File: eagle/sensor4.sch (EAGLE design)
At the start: 16 parts, among them X1 1503_02, X3 1503_02

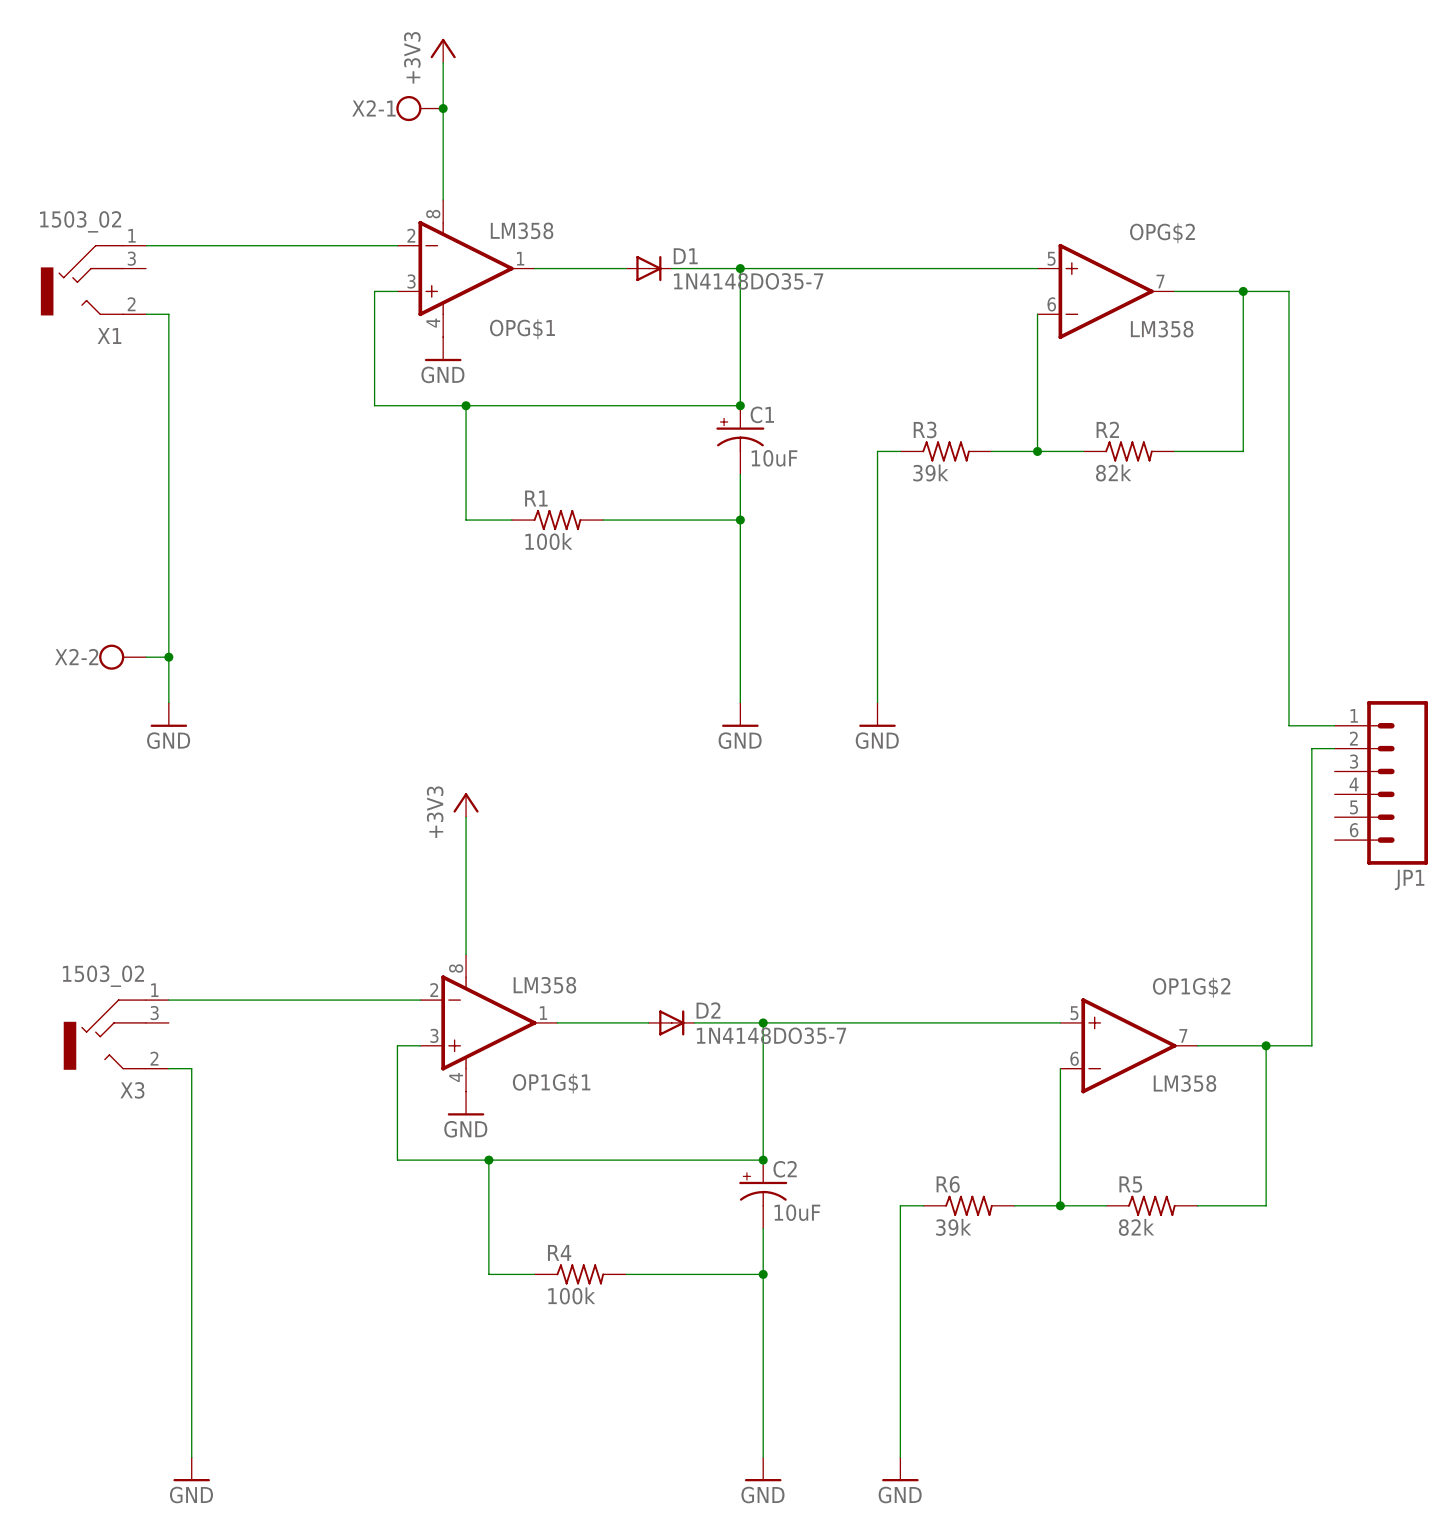
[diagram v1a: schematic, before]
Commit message: Replace two LM358s with one LMV324
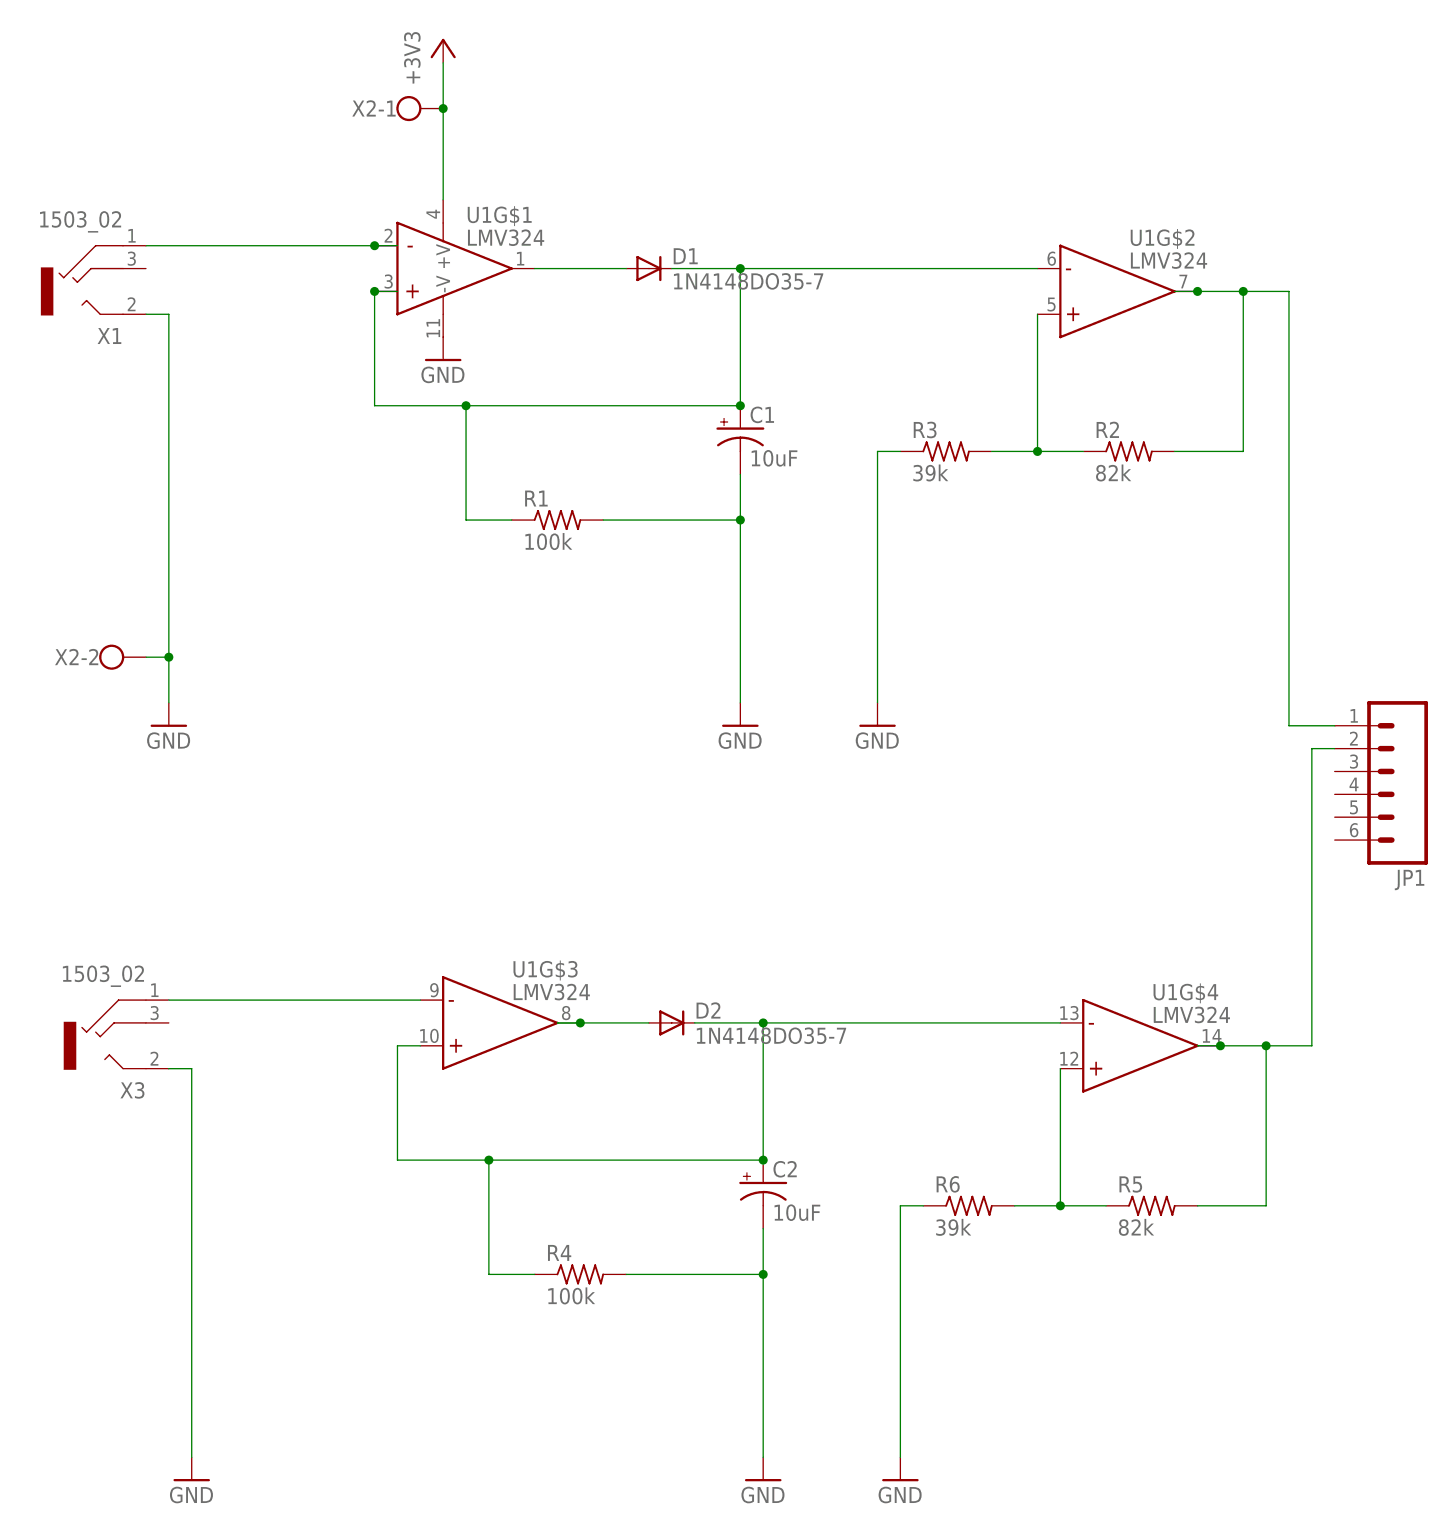
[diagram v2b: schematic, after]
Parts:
- removed OP, OP1: LM358, SparkFun-AnalogIC:LM358
- added U1: LMV324, SparkFun-AnalogIC:LMV324
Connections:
- net +3V3: now also U1G$1.+V; no longer OP1G$1.V+, OPG$1.V+
- net GND: now also U1G$1.-V; no longer OP1G$1.V-, OPG$1.V-
- net N$1: now also U1G$1.OUT; no longer OPG$1.OUT
- net N$10: now also U1G$4.OUT; no longer OP1G$2.OUT
- net N$2: now also U1G$1.+IN, U1G$2.-IN; no longer OPG$1.+IN, OPG$2.+IN
- net N$3: now also U1G$3.OUT; no longer OP1G$1.OUT
- net N$4: now also U1G$3.+IN, U1G$4.-IN; no longer OP1G$1.+IN, OP1G$2.+IN
- net N$5: now also U1G$2.+IN; no longer OPG$2.-IN
- net N$6: now also U1G$1.-IN; no longer OPG$1.-IN
- net N$7: now also U1G$2.OUT; no longer OPG$2.OUT
- net N$8: now also U1G$4.+IN; no longer OP1G$2.-IN
- net N$9: now also U1G$3.-IN; no longer OP1G$1.-IN
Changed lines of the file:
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@@
 </classes>
 <parts>
-<part name="OP" library="SparkFun-AnalogIC" deviceset="LM358" device=""/>
 <part name="C1" library="resistor" deviceset="CPOL-US" device="E2.5-5" value="10uF"/>
 <part name="R1" library="resistor" deviceset="R-US_" device="0207/10" value="100k"/>
@@
 <part name="GND4" library="supply1" deviceset="GND" device=""/>
 <part name="X1" library="con-lumberg" deviceset="1503_02" device=""/>
-<part name="OP1" library="SparkFun-AnalogIC" deviceset="LM358" device=""/>
 <part name="C2" library="resistor" deviceset="CPOL-US" device="E2.5-5" value="10uF"/>
 <part name="R4" library="resistor" deviceset="R-US_" device="0207/10" value="100k"/>
@@
 <part name="R6" library="resistor" deviceset="R-US_" device="0207/10" value="39k"/>
 <part name="D2" library="diode" deviceset="1N4148" device="DO35-7"/>
-<part name="+3V1" library="supply1" deviceset="+3V3" device=""/>
 <part name="GND5" library="supply1" deviceset="GND" device=""/>
 <part name="GND6" library="supply1" deviceset="GND" device=""/>
-<part name="GND7" library="supply1" deviceset="GND" device=""/>
 <part name="GND8" library="supply1" deviceset="GND" device=""/>
 <part name="X3" library="con-lumberg" deviceset="1503_02" device=""/>
 <part name="X2" library="con-wago-500" deviceset="W237-102" device=""/>
 <part name="JP1" library="SparkFun-Connectors" deviceset="M06" device="SIP"/>
+<part name="U1" library="SparkFun-AnalogIC" deviceset="LMV324" device="" value="LMV324"/>
 </parts>
 <sheets>
@@
 </plain>
 <instances>
-<instance part="OP" gate="G$1" x="43.18" y="71.12"/>
-<instance part="OP" gate="G$2" x="116.84" y="68.58"/>
 <instance part="C1" gate="G$1" x="76.2" y="53.34"/>
 <instance part="R1" gate="G$1" x="55.88" y="43.18"/>
@@
 <instance part="GND4" gate="1" x="12.7" y="20.32"/>
 <instance part="X1" gate="G$1" x="5.08" y="68.58" rot="R180"/>
-<instance part="OP1" gate="G$1" x="45.72" y="-12.7"/>
-<instance part="OP1" gate="G$2" x="119.38" y="-15.24"/>
 <instance part="C2" gate="G$1" x="78.74" y="-30.48"/>
 <instance part="R4" gate="G$1" x="58.42" y="-40.64"/>
@@
 <instance part="R6" gate="G$1" x="101.6" y="-33.02"/>
 <instance part="D2" gate="G$1" x="68.58" y="-12.7"/>
-<instance part="+3V1" gate="G$1" x="45.72" y="12.7"/>
 <instance part="GND5" gate="1" x="78.74" y="-63.5"/>
 <instance part="GND6" gate="1" x="93.98" y="-63.5"/>
-<instance part="GND7" gate="1" x="45.72" y="-22.86"/>
 <instance part="GND8" gate="1" x="15.24" y="-63.5"/>
 <instance part="X3" gate="G$1" x="7.62" y="-15.24" rot="R180"/>
@@
 <instance part="X2" gate="-2" x="5.08" y="27.94"/>
 <instance part="JP1" gate="G$1" x="147.32" y="15.24" rot="R180"/>
+<instance part="U1" gate="G$1" x="38.1" y="71.12"/>
+<instance part="U1" gate="G$2" x="111.76" y="68.58"/>
+<instance part="U1" gate="G$3" x="43.18" y="-12.7"/>
+<instance part="U1" gate="G$4" x="114.3" y="-15.24"/>
 </instances>
 <busses>
@@
 <nets>
 <net name="GND" class="0">
-<segment>
-<pinref part="OP" gate="G$1" pin="V-"/>
-<pinref part="GND3" gate="1" pin="GND"/>
-</segment>
 <segment>
 <pinref part="R1" gate="G$1" pin="2"/>
@@
 </segment>
 <segment>
-<pinref part="OP1" gate="G$1" pin="V-"/>
-<pinref part="GND7" gate="1" pin="GND"/>
-</segment>
-<segment>
 <pinref part="R4" gate="G$1" pin="2"/>
 <wire x1="63.5" y1="-40.64" x2="78.74" y2="-40.64" width="0.1524" layer="91"/>
@@
 <pinref part="X3" gate="G$1" pin="2"/>
 </segment>
+<segment>
+<pinref part="GND3" gate="1" pin="GND"/>
+<pinref part="U1" gate="G$1" pin="-V"/>
+</segment>
 </net>
 <net name="N$1" class="0">
 <segment>
-<pinref part="OP" gate="G$1" pin="OUT"/>
 <pinref part="D1" gate="G$1" pin="A"/>
 <wire x1="53.34" y1="71.12" x2="63.5" y2="71.12" width="0.1524" layer="91"/>
+<pinref part="U1" gate="G$1" pin="OUT"/>
 </segment>
 </net>
@@
 <wire x1="45.72" y1="55.88" x2="35.56" y2="55.88" width="0.1524" layer="91"/>
 <wire x1="35.56" y1="55.88" x2="35.56" y2="68.58" width="0.1524" layer="91"/>
-<pinref part="OP" gate="G$1" pin="+IN"/>
 <wire x1="35.56" y1="68.58" x2="38.1" y2="68.58" width="0.1524" layer="91"/>
 <pinref part="R1" gate="G$1" pin="1"/>
@@
 <junction x="76.2" y="71.12"/>
 <junction x="76.2" y="55.88"/>
-<pinref part="OP" gate="G$2" pin="+IN"/>
 <wire x1="76.2" y1="71.12" x2="109.22" y2="71.12" width="0.1524" layer="91"/>
+<pinref part="U1" gate="G$1" pin="+IN"/>
+<junction x="35.56" y="68.58"/>
+<pinref part="U1" gate="G$2" pin="-IN"/>
 </segment>
 </net>
@@
 <pinref part="R3" gate="G$1" pin="2"/>
 <wire x1="114.3" y1="50.8" x2="109.22" y2="50.8" width="0.1524" layer="91"/>
-<pinref part="OP" gate="G$2" pin="-IN"/>
 <wire x1="109.22" y1="50.8" x2="104.14" y2="50.8" width="0.1524" layer="91"/>
 <wire x1="109.22" y1="66.04" x2="109.22" y2="50.8" width="0.1524" layer="91"/>
 <junction x="109.22" y="50.8"/>
+<pinref part="U1" gate="G$2" pin="+IN"/>
 </segment>
 </net>
 <net name="+3V3" class="0">
 <segment>
-<pinref part="OP" gate="G$1" pin="V+"/>
 <pinref part="+3V2" gate="G$1" pin="+3V3"/>
 <wire x1="43.18" y1="78.74" x2="43.18" y2="88.9" width="0.1524" layer="91"/>
@@
 <wire x1="43.18" y1="88.9" x2="43.18" y2="93.98" width="0.1524" layer="91"/>
 <junction x="43.18" y="88.9"/>
-</segment>
-<segment>
-<pinref part="OP1" gate="G$1" pin="V+"/>
-<pinref part="+3V1" gate="G$1" pin="+3V3"/>
-<wire x1="45.72" y1="-5.08" x2="45.72" y2="10.16" width="0.1524" layer="91"/>
+<pinref part="U1" gate="G$1" pin="+V"/>
 </segment>
 </net>
 <net name="N$6" class="0">
 <segment>
-<pinref part="OP" gate="G$1" pin="-IN"/>
-<wire x1="10.16" y1="73.66" x2="38.1" y2="73.66" width="0.1524" layer="91"/>
+<wire x1="10.16" y1="73.66" x2="35.56" y2="73.66" width="0.1524" layer="91"/>
 <pinref part="X1" gate="G$1" pin="1"/>
+<pinref part="U1" gate="G$1" pin="-IN"/>
+<wire x1="35.56" y1="73.66" x2="38.1" y2="73.66" width="0.1524" layer="91"/>
+<junction x="35.56" y="73.66"/>
 </segment>
 </net>
 <net name="N$7" class="0">
 <segment>
-<pinref part="OP" gate="G$2" pin="OUT"/>
-<wire x1="124.46" y1="68.58" x2="132.08" y2="68.58" width="0.1524" layer="91"/>
+<wire x1="124.46" y1="68.58" x2="127" y2="68.58" width="0.1524" layer="91"/>
+<wire x1="127" y1="68.58" x2="132.08" y2="68.58" width="0.1524" layer="91"/>
 <wire x1="132.08" y1="68.58" x2="132.08" y2="50.8" width="0.1524" layer="91"/>
 <pinref part="R2" gate="G$1" pin="2"/>
@@
 <wire x1="142.24" y1="20.32" x2="137.16" y2="20.32" width="0.1524" layer="91"/>
 <wire x1="137.16" y1="20.32" x2="137.16" y2="68.58" width="0.1524" layer="91"/>
+<pinref part="U1" gate="G$2" pin="OUT"/>
+<junction x="127" y="68.58"/>
 </segment>
 </net>
 <net name="N$3" class="0">
 <segment>
-<pinref part="OP1" gate="G$1" pin="OUT"/>
 <pinref part="D2" gate="G$1" pin="A"/>
-<wire x1="55.88" y1="-12.7" x2="66.04" y2="-12.7" width="0.1524" layer="91"/>
+<wire x1="55.88" y1="-12.7" x2="58.42" y2="-12.7" width="0.1524" layer="91"/>
+<pinref part="U1" gate="G$3" pin="OUT"/>
+<wire x1="58.42" y1="-12.7" x2="66.04" y2="-12.7" width="0.1524" layer="91"/>
+<junction x="58.42" y="-12.7"/>
 </segment>
 </net>
@@
 <wire x1="48.26" y1="-27.94" x2="38.1" y2="-27.94" width="0.1524" layer="91"/>
 <wire x1="38.1" y1="-27.94" x2="38.1" y2="-15.24" width="0.1524" layer="91"/>
-<pinref part="OP1" gate="G$1" pin="+IN"/>
 <wire x1="38.1" y1="-15.24" x2="40.64" y2="-15.24" width="0.1524" layer="91"/>
 <pinref part="R4" gate="G$1" pin="1"/>
@@
 <junction x="78.74" y="-12.7"/>
 <junction x="78.74" y="-27.94"/>
-<pinref part="OP1" gate="G$2" pin="+IN"/>
 <wire x1="78.74" y1="-12.7" x2="111.76" y2="-12.7" width="0.1524" layer="91"/>
+<pinref part="U1" gate="G$3" pin="+IN"/>
+<pinref part="U1" gate="G$4" pin="-IN"/>
 </segment>
 </net>
@@
 <pinref part="R6" gate="G$1" pin="2"/>
 <wire x1="116.84" y1="-33.02" x2="111.76" y2="-33.02" width="0.1524" layer="91"/>
-<pinref part="OP1" gate="G$2" pin="-IN"/>
 <wire x1="111.76" y1="-33.02" x2="106.68" y2="-33.02" width="0.1524" layer="91"/>
 <wire x1="111.76" y1="-17.78" x2="111.76" y2="-33.02" width="0.1524" layer="91"/>
 <junction x="111.76" y="-33.02"/>
+<pinref part="U1" gate="G$4" pin="+IN"/>
 </segment>
 </net>
 <net name="N$9" class="0">
 <segment>
-<pinref part="OP1" gate="G$1" pin="-IN"/>
 <wire x1="12.7" y1="-10.16" x2="40.64" y2="-10.16" width="0.1524" layer="91"/>
 <pinref part="X3" gate="G$1" pin="1"/>
+<pinref part="U1" gate="G$3" pin="-IN"/>
 </segment>
 </net>
 <net name="N$10" class="0">
 <segment>
-<pinref part="OP1" gate="G$2" pin="OUT"/>
-<wire x1="127" y1="-15.24" x2="134.62" y2="-15.24" width="0.1524" layer="91"/>
+<wire x1="127" y1="-15.24" x2="129.54" y2="-15.24" width="0.1524" layer="91"/>
+<wire x1="129.54" y1="-15.24" x2="134.62" y2="-15.24" width="0.1524" layer="91"/>
 <wire x1="134.62" y1="-15.24" x2="134.62" y2="-33.02" width="0.1524" layer="91"/>
 <pinref part="R5" gate="G$1" pin="2"/>
@@
 <wire x1="142.24" y1="17.78" x2="139.7" y2="17.78" width="0.1524" layer="91"/>
 <wire x1="139.7" y1="17.78" x2="139.7" y2="-15.24" width="0.1524" layer="91"/>
-</segment>
-</net>
+<pinref part="U1" gate="G$4" pin="OUT"/>
+<junction x="129.54" y="-15.24"/>
+</segment>
+</net>
